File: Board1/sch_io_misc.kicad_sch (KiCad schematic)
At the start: 9 parts, among them J4 Cool. Plate, J5 OLED, J6 Rotary Encoder, J9 IR Therm

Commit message: v1.2 release of board with bug fixes etc
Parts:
- J4: value Cool. Plate -> Cool.Plate
- J6: value Rotary Encoder -> Rot.Encoder
- J9: value IR Therm -> IRTherm
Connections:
- net ROTARY_BTN: now also J6.3 (Pin_3); no longer J6.5 (Pin_5)
- net ROTARY_SIG: now also J6.5 (Pin_5); no longer J6.3 (Pin_3)
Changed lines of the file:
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@@
 (kicad_sch
-	(version 20231120)
+	(version 20250114)
 	(generator "eeschema")
-	(generator_version "8.0")
+	(generator_version "9.0")
 	(paper "A4")
 	(title_block
 		(title "Misc I/O")
-		(date "2025-02-19")
-		(rev "1.1")
+		(date "2025-03-08")
+		(rev "1.2")
 		(company "Wattle Labs")
+	)
+	(rectangle
+		(start 99.06 125.73)
+		(end 99.06 125.73)
+		(stroke
+			(width 0)
+			(type default)
+		)
+		(fill
+			(type none)
+		)
+	)
+	(text "OLED Connector"
+		(exclude_from_sim no)
+		(at 40.64 96.774 0)
+		(effects
+			(font
+				(size 1.27 1.27)
+			)
+		)
+	)
+	(text "Rotary Encoder Connector"
+		(exclude_from_sim no)
+		(at 45.72 37.846 0)
+		(effects
+			(font
+				(size 1.27 1.27)
+			)
+		)
+	)
+	(text "Cooling Plate LED Connector"
+		(exclude_from_sim no)
+		(at 104.14 37.846 0)
+		(effects
+			(font
+				(size 1.27 1.27)
+			)
+		)
+	)
+	(text "Cooling Plate IR Thermometer Connector"
+		(exclude_from_sim no)
+		(at 172.466 37.846 0)
+		(effects
+			(font
+				(size 1.27 1.27)
+			)
+		)
+	)
+	(text "Buzzer"
+		(exclude_from_sim no)
+		(at 93.472 97.028 0)
+		(effects
+			(font
+				(size 1.27 1.27)
+			)
+		)
+	)
+	(text_box "DESIGN NOTE:\n\nLEDs live on a seperate schematic/PCB (board 2)"
+		(exclude_from_sim no)
+		(at 88.9 71.12 0)
+		(size 53.34 10.16)
+		(margins 1.2025 1.2025 1.2025 1.2025)
+		(stroke
+			(width 0.5)
+			(type solid)
+			(color 200 200 200 1)
+		)
+		(fill
+			(type none)
+		)
+		(effects
+			(font
+				(size 1.27 1.27)
+				(color 0 0 0 1)
+			)
+			(justify left top)
+		)
+	)
+	(text_box "DESIGN NOTE:\n\nSSD1306 128X64 pixel 1.5\" OLED"
+		(exclude_from_sim no)
+		(at 33.02 127 0)
+		(size 38.1 10.16)
+		(margins 1.2025 1.2025 1.2025 1.2025)
+		(stroke
+			(width 0.5)
+			(type solid)
+			(color 200 200 200 1)
+		)
+		(fill
+			(type none)
+		)
+		(effects
+			(font
+				(size 1.27 1.27)
+				(color 0 0 0 1)
+			)
+			(justify left top)
+		)
+	)
+	(text_box "DESIGN NOTE:\n\nEncoder module includes pullups"
+		(exclude_from_sim no)
+		(at 33.02 71.12 0)
+		(size 38.1 10.16)
+		(margins 1.2025 1.2025 1.2025 1.2025)
+		(stroke
+			(width 0.5)
+			(type solid)
+			(color 200 200 200 1)
+		)
+		(fill
+			(type none)
+		)
+		(effects
+			(font
+				(size 1.27 1.27)
+				(color 0 0 0 1)
+			)
+			(justify left top)
+		)
+	)
+	(text_box "[${#}] ${TITLE}"
+		(exclude_from_sim no)
+		(at 12.065 12.065 0)
+		(size 273.05 13.335)
+		(margins 2.2499 2.2499 2.2499 2.2499)
+		(stroke
+			(width -0.0001)
+			(type default)
+		)
+		(fill
+			(type none)
+		)
+		(effects
+			(font
+				(size 3 3)
+				(thickness 0.375)
+			)
+		)
 	)
 	(junction
@@
 	(wire
 		(pts
+			(xy 43.18 53.34) (xy 50.8 53.34)
+		)
+		(stroke
+			(width 0)
+			(type default)
+		)
+	)
+	(wire
+		(pts
 			(xy 43.18 60.96) (xy 52.07 60.96)
 		)
@@
 	(wire
 		(pts
-			(xy 43.18 53.34) (xy 50.8 53.34)
-		)
-		(stroke
-			(width 0)
-			(type default)
-		)
-	)
-	(wire
-		(pts
 			(xy 49.53 118.11) (xy 52.07 118.11)
 		)
@@
 	(wire
 		(pts
+			(xy 43.18 55.88) (xy 52.07 55.88)
+		)
+		(stroke
+			(width 0)
+			(type default)
+		)
+	)
+	(wire
+		(pts
 			(xy 167.64 60.96) (xy 167.64 62.23)
 		)
@@
 	(wire
 		(pts
+			(xy 43.18 58.42) (xy 52.07 58.42)
+		)
+		(stroke
+			(width 0)
+			(type default)
+		)
+	)
+	(wire
+		(pts
 			(xy 97.79 110.49) (xy 97.79 113.03)
 		)
@@
 	(wire
 		(pts
-			(xy 43.18 55.88) (xy 52.07 55.88)
-		)
-		(stroke
-			(width 0)
-			(type default)
-		)
-	)
-	(wire
-		(pts
 			(xy 49.53 105.41) (xy 49.53 113.03)
 		)
@@
 	(wire
 		(pts
-			(xy 43.18 58.42) (xy 52.07 58.42)
-		)
-		(stroke
-			(width 0)
-			(type default)
-		)
-	)
-	(wire
-		(pts
 			(xy 116.84 49.53) (xy 119.38 49.53)
 		)
@@
 			(width 0)
 			(type default)
-		)
-	)
-	(rectangle
-		(start 99.06 125.73)
-		(end 99.06 125.73)
-		(stroke
-			(width 0)
-			(type default)
-		)
-		(fill
-			(type none)
-		)
-	)
-	(text_box "DESIGN NOTE:\n\nLEDs live on a seperate schematic/PCB (board 2)"
-		(exclude_from_sim no)
-		(at 88.9 71.12 0)
-		(size 53.34 10.16)
-		(stroke
-			(width 0.5)
-			(type solid)
-			(color 200 200 200 1)
-		)
-		(fill
-			(type none)
-		)
-		(effects
-			(font
-				(size 1.27 1.27)
-				(color 0 0 0 1)
-			)
-			(justify left top)
-		)
-	)
-	(text_box "DESIGN NOTE:\n\nSSD1306 128X64 pixel 1.5\" OLED"
-		(exclude_from_sim no)
-		(at 33.02 127 0)
-		(size 38.1 10.16)
-		(stroke
-			(width 0.5)
-			(type solid)
-			(color 200 200 200 1)
-		)
-		(fill
-			(type none)
-		)
-		(effects
-			(font
-				(size 1.27 1.27)
-				(color 0 0 0 1)
-			)
-			(justify left top)
-		)
-	)
-	(text_box "DESIGN NOTE:\n\nEncoder module includes pullups"
-		(exclude_from_sim no)
-		(at 33.02 71.12 0)
-		(size 38.1 10.16)
-		(stroke
-			(width 0.5)
-			(type solid)
-			(color 200 200 200 1)
-		)
-		(fill
-			(type none)
-		)
-		(effects
-			(font
-				(size 1.27 1.27)
-				(color 0 0 0 1)
-			)
-			(justify left top)
-		)
-	)
-	(text_box "[${#}] ${TITLE}"
-		(exclude_from_sim no)
-		(at 12.065 12.065 0)
-		(size 273.05 13.335)
-		(stroke
-			(width -0.0001)
-			(type default)
-		)
-		(fill
-			(type none)
-		)
-		(effects
-			(font
-				(size 3 3)
-				(thickness 0.375)
-			)
-		)
-	)
-	(text "OLED Connector"
-		(exclude_from_sim no)
-		(at 40.64 96.774 0)
-		(effects
-			(font
-				(size 1.27 1.27)
-			)
-		)
-	)
-	(text "Rotary Encoder Connector"
-		(exclude_from_sim no)
-		(at 45.72 37.846 0)
-		(effects
-			(font
-				(size 1.27 1.27)
-			)
-		)
-	)
-	(text "Cooling Plate LED Connector"
-		(exclude_from_sim no)
-		(at 104.14 37.846 0)
-		(effects
-			(font
-				(size 1.27 1.27)
-			)
-		)
-	)
-	(text "Cooling Plate IR Thermometer Connector"
-		(exclude_from_sim no)
-		(at 172.466 37.846 0)
-		(effects
-			(font
-				(size 1.27 1.27)
-			)
-		)
-	)
-	(text "Buzzer"
-		(exclude_from_sim no)
-		(at 93.472 97.028 0)
-		(effects
-			(font
-				(size 1.27 1.27)
-			)
 		)
 	)
 	(global_label "ROTARY_SIG"
 		(shape input)
-		(at 52.07 55.88 0)
+		(at 52.07 60.96 0)
 		(fields_autoplaced yes)
 		(effects
@@
 		)
 		(property "Intersheetrefs" "${INTERSHEET_REFS}"
-			(at 65.4682 55.88 0)
+			(at 65.4682 60.96 0)
 			(effects
 				(font
@@
 	(global_label "ROTARY_BTN"
 		(shape input)
-		(at 52.07 60.96 0)
+		(at 52.07 55.88 0)
 		(fields_autoplaced yes)
 		(effects
@@
 		)
 		(property "Intersheetrefs" "${INTERSHEET_REFS}"
-			(at 65.952 60.96 0)
+			(at 65.952 55.88 0)
 			(effects
 				(font
@@
 			)
 		)
-		(property "Value" "Rotary Encoder"
+		(property "Value" "Rot.Encoder"
 			(at 40.64 47.752 0)
 			(effects
@@
 			)
 		)
-		(property "Value" "Cool. Plate"
+		(property "Value" "Cool.Plate"
 			(at 125.73 53.3399 0)
 			(effects
@@
 			)
 		)
-		(property "Value" "IR Therm"
+		(property "Value" "IRTherm"
 			(at 176.53 55.8799 0)
 			(effects

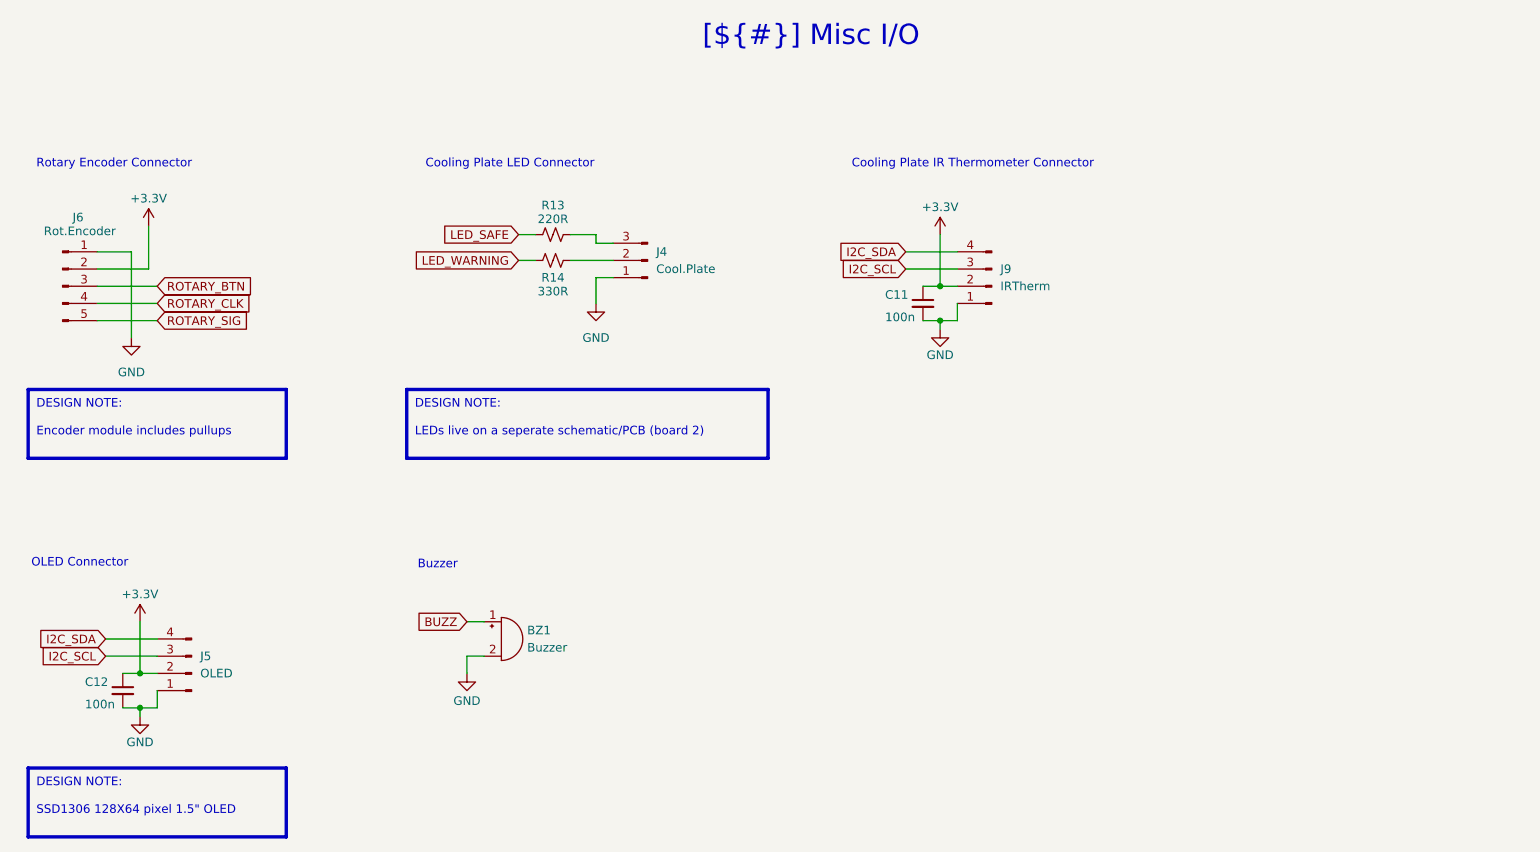
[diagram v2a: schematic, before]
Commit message: Tweaks to schematic for clarity and minor firmware
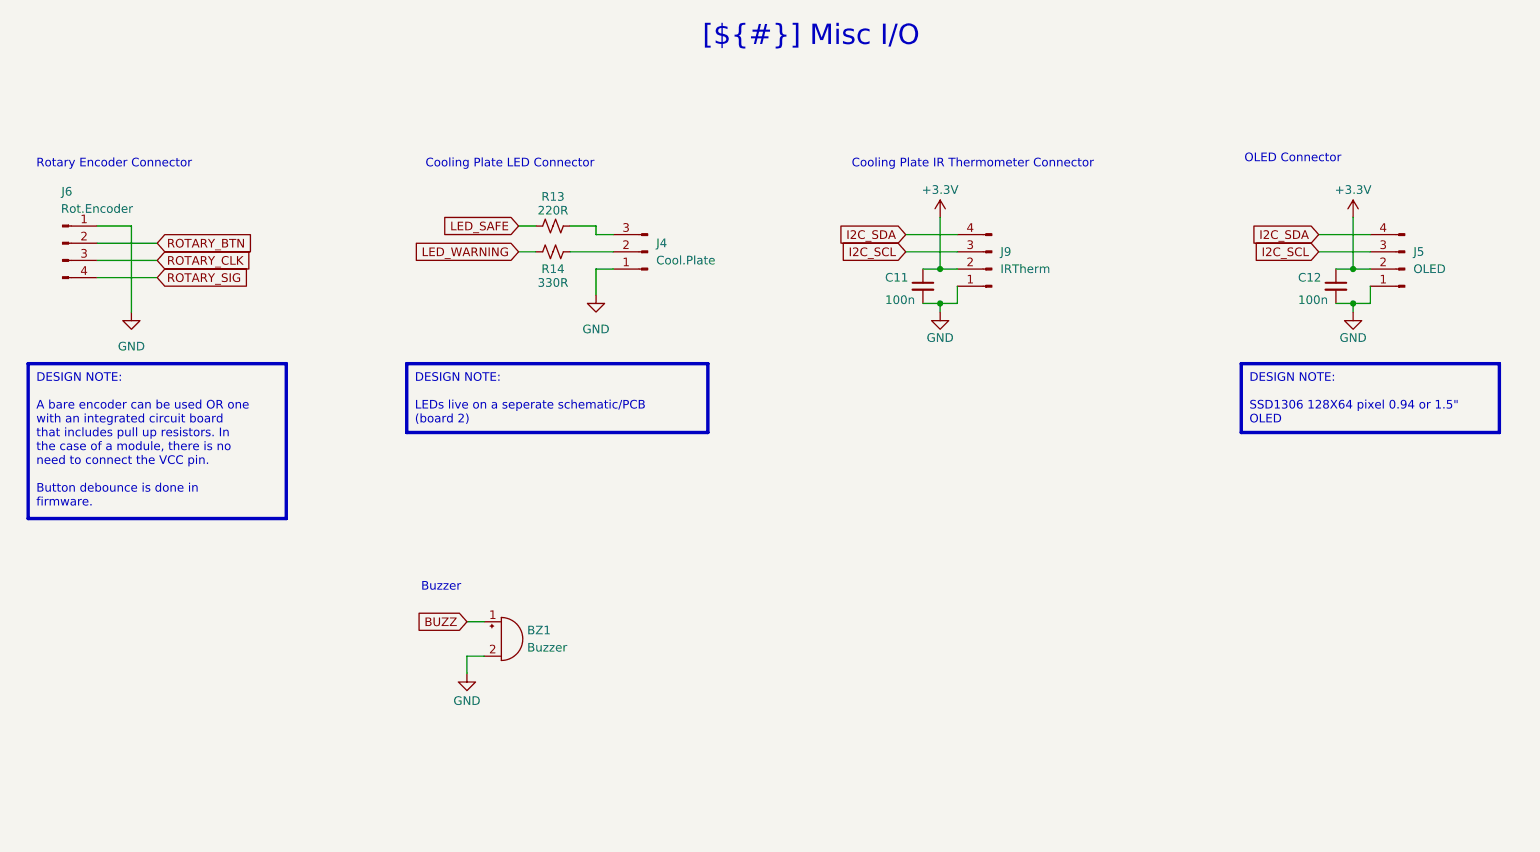
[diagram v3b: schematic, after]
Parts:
- removed J6: Rot.Encoder, Connector_PinHeader_2.54mm:PinHeader_1x05_P2.54mm_Vertical, symbol Connector:Conn_01x05_Pin
- added J6: Rot.Encoder, Connector_PinHeader_2.54mm:PinHeader_1x04_P2.54mm_Vertical, symbol Connector:Conn_01x04_Pin
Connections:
- net GND: now also J6.1 (Pin_1)
- net ROTARY_BTN: now also J6.2 (Pin_2)
- net ROTARY_CLK: now also J6.3 (Pin_3)
- net ROTARY_SIG: now also J6.4 (Pin_4)
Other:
- moved on the sheet: C11, C12, J4, J5, J9, R13, R14
